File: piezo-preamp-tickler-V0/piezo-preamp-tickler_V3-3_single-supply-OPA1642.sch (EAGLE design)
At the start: 62 parts, among them IC1 OPA2134UA, Q2 MMBFJ201, SW2-SPST INPUT-select

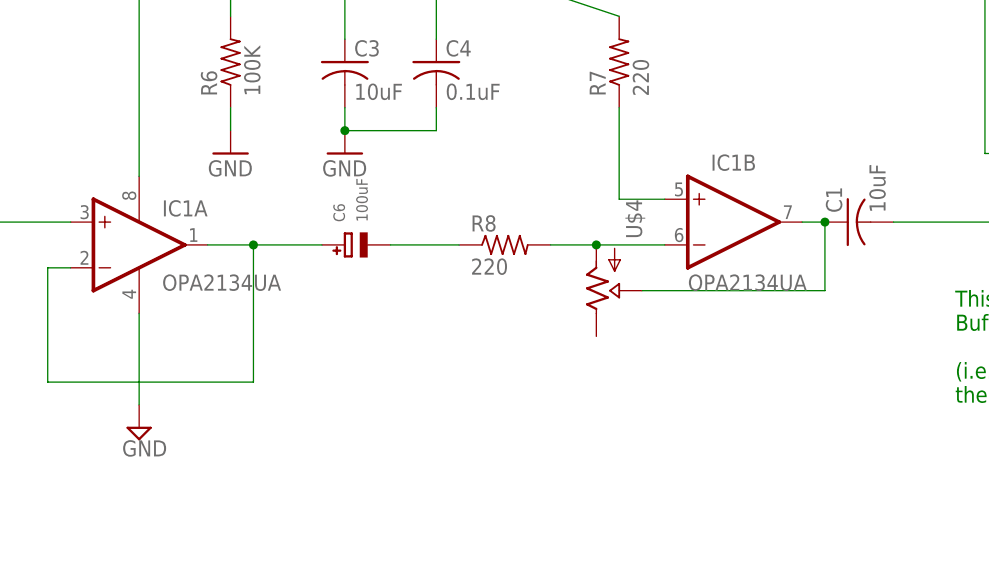
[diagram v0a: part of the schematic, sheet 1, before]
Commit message: piezo preamp fixes
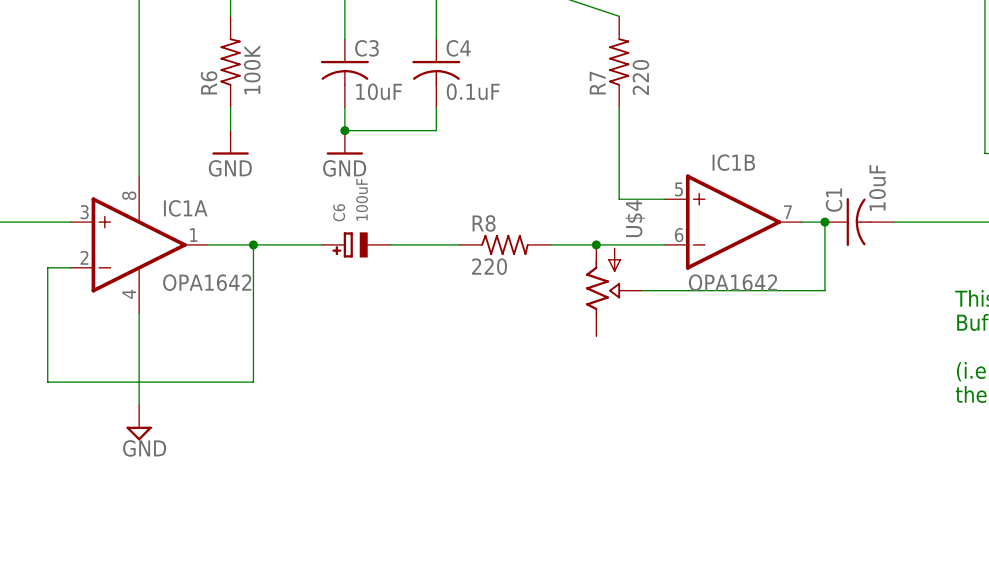
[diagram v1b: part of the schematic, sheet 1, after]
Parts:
- IC1: value OPA2134UA -> OPA1642
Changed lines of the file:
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@@
 <part name="TO-PHONE" library="Daniel" deviceset="AUDIO-JACK3" device="LGPADS"/>
 <part name="TO-HEADSET" library="Daniel" deviceset="AUDIO-JACK3" device="LGPADS"/>
-<part name="IC1" library="linear" library_urn="urn:adsk.eagle:library:262" deviceset="OPA2*" device="UA" technology="134" value="OPA2134UA"/>
+<part name="IC1" library="linear" library_urn="urn:adsk.eagle:library:262" deviceset="OPA2*" device="UA" technology="134" value="OPA1642"/>
 <part name="PIEZO" library="adafruit" deviceset="JST_2PIN" device="-THM"/>
 <part name="LED1" library="led" library_urn="urn:adsk.eagle:library:259" deviceset="LED" device="3MM"/>

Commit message: piezo preamp updates
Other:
- note removed: "Power"
- moved on the sheet: C2, L1
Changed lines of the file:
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@@
 <text x="-88.9" y="76.2" size="1.778" layer="91">"A Discrete FET Guitar Preamp" by J. Donald Tillman</text>
 <text x="160.02" y="53.34" size="1.778" layer="91">"Simple JFET Preamp for an iDevice Guitar Interface"</text>
-<wire x1="7.62" y1="162.56" x2="-53.34" y2="162.56" width="0.1524" layer="98"/>
-<wire x1="-53.34" y1="162.56" x2="-53.34" y2="127" width="0.1524" layer="98"/>
-<wire x1="-53.34" y1="127" x2="7.62" y2="127" width="0.1524" layer="98"/>
-<wire x1="7.62" y1="127" x2="7.62" y2="162.56" width="0.1524" layer="98"/>
-<text x="-15.24" y="154.94" size="5.08" layer="91">Power</text>
 <text x="299.72" y="45.72" size="1.778" layer="91">T - Left
 R1 - Right
@@
 <attribute name="VALUE" x="264.922" y="32.512" size="1.778" layer="96"/>
 </instance>
-<instance part="C2" gate="G$1" x="-17.78" y="142.24"/>
+<instance part="C2" gate="G$1" x="81.28" y="66.04"/>
 <instance part="C1" gate="G$1" x="99.06" y="30.48" rot="R90"/>
 <instance part="C3" gate="G$1" x="43.18" y="48.26"/>
 <instance part="R14" gate="G$1" x="-60.96" y="38.1"/>
-<instance part="P+3" gate="1" x="-48.26" y="157.48"/>
+<instance part="P+3" gate="1" x="101.6" y="81.28"/>
 <instance part="Q2" gate="G$1" x="193.04" y="33.02"/>
 <instance part="SUPPLY3" gate="GND" x="20.32" y="7.62"/>
 <instance part="SUPPLY4" gate="GND" x="-71.12" y="12.7"/>
-<instance part="SUPPLY5" gate="GND" x="-17.78" y="132.08"/>
+<instance part="SUPPLY5" gate="GND" x="81.28" y="53.34"/>
 <instance part="R13" gate="G$1" x="-45.72" y="45.72" rot="R270"/>
 <instance part="U$2" gate="G$1" x="132.08" y="38.1"/>
@@
 <instance part="C4" gate="G$1" x="53.34" y="48.26"/>
 <instance part="C6" gate="G$1" x="45.72" y="27.94" rot="R90"/>
-<instance part="L1" gate="G$1" x="-30.48" y="147.32" rot="R90"/>
+<instance part="L1" gate="G$1" x="93.98" y="73.66" rot="R270"/>
 <instance part="U$1" gate="G$1" x="279.4" y="0" rot="R180"/>
 </instances>
@@
 <pinref part="C2" gate="G$1" pin="2"/>
 <pinref part="SUPPLY5" gate="GND" pin="GND"/>
-<wire x1="-17.78" y1="137.16" x2="-17.78" y2="134.62" width="0.1524" layer="91"/>
+<wire x1="81.28" y1="60.96" x2="81.28" y2="55.88" width="0.1524" layer="91"/>
 </segment>
 </net>
@@
 <segment>
 <pinref part="P+3" gate="1" pin="+12V"/>
-<wire x1="-48.26" y1="154.94" x2="-48.26" y2="147.32" width="0.1524" layer="91"/>
+<wire x1="101.6" y1="78.74" x2="101.6" y2="73.66" width="0.1524" layer="91"/>
 <pinref part="L1" gate="G$1" pin="1"/>
-<wire x1="-48.26" y1="147.32" x2="-38.1" y2="147.32" width="0.1524" layer="91"/>
 </segment>
 </net>
@@
 <segment>
 <pinref part="C2" gate="G$1" pin="1"/>
-<wire x1="-17.78" y1="147.32" x2="-17.78" y2="144.78" width="0.1524" layer="91"/>
+<wire x1="81.28" y1="73.66" x2="81.28" y2="68.58" width="0.1524" layer="91"/>
 <wire x1="30.48" y1="68.58" x2="20.32" y2="68.58" width="0.1524" layer="91"/>
 <wire x1="20.32" y1="35.56" x2="20.32" y2="68.58" width="0.1524" layer="91"/>
 <pinref part="R5" gate="G$1" pin="2"/>
 <pinref part="IC1" gate="A" pin="V+"/>
-<wire x1="20.32" y1="68.58" x2="-7.62" y2="68.58" width="0.1524" layer="91"/>
 <junction x="20.32" y="68.58"/>
-<wire x1="-17.78" y1="147.32" x2="-7.62" y2="147.32" width="0.1524" layer="91"/>
-<wire x1="-7.62" y1="147.32" x2="-7.62" y2="68.58" width="0.1524" layer="91"/>
+<wire x1="81.28" y1="73.66" x2="20.32" y2="73.66" width="0.1524" layer="91"/>
+<wire x1="20.32" y1="73.66" x2="20.32" y2="68.58" width="0.1524" layer="91"/>
 <pinref part="D4" gate="G$1" pin="C2"/>
 <wire x1="-38.1" y1="43.18" x2="-38.1" y2="68.58" width="0.1524" layer="91"/>
-<wire x1="-38.1" y1="68.58" x2="-7.62" y2="68.58" width="0.1524" layer="91"/>
-<junction x="-7.62" y="68.58"/>
+<wire x1="-38.1" y1="68.58" x2="20.32" y2="68.58" width="0.1524" layer="91"/>
+<junction x="20.32" y="68.58"/>
 <pinref part="L1" gate="G$1" pin="2"/>
-<wire x1="-17.78" y1="147.32" x2="-22.86" y2="147.32" width="0.1524" layer="91"/>
-<junction x="-17.78" y="147.32"/>
-</segment>
-</net>
+<wire x1="81.28" y1="73.66" x2="86.36" y2="73.66" width="0.1524" layer="91"/>
+<junction x="81.28" y="73.66"/>
+</segment>
+</net>

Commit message: piezo preamp updates
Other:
- moved on the sheet: BATTERY1, C10, C12, J1, LED2, LED3, POWER, R20, R21, R22, R23, R24

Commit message: piezo preamp updates
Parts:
- L1: value (none) -> 100uH
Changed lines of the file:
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@@
 <part name="C4" library="adafruit" deviceset="C-US" device="C0805K" value="0.1uF"/>
 <part name="C6" library="microbuilder" deviceset="CAP_TANTALUM" device="A/3216_REFLOW" value="100uF"/>
-<part name="L1" library="rcl" library_urn="urn:adsk.eagle:library:334" deviceset="L-US" device="L3225P" package3d_urn="urn:adsk.eagle:package:23479/1"/>
+<part name="L1" library="rcl" library_urn="urn:adsk.eagle:library:334" deviceset="L-US" device="L3225P" package3d_urn="urn:adsk.eagle:package:23479/1" value="100uH"/>
 <part name="U$1" library="CMU-ArtFab" deviceset="TRS-1/8&quot;-3.5MM" device=""/>
 <part name="U$5" library="CMU-ArtFab" deviceset="TPS7A49" device=""/>
